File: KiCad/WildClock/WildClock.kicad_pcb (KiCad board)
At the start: 2 copper layers, 70 x 70 mm, 37 parts, among them Q1 AO3401A, Q2 AO3401A, Q3 AO3401A, Q4 AO3401A, Q5 AO3400A, SW1 SWUP, SW2 SWDOWN, SW3 SWOK, U1 ESP32-C3-MINI-1, U3 74HC595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

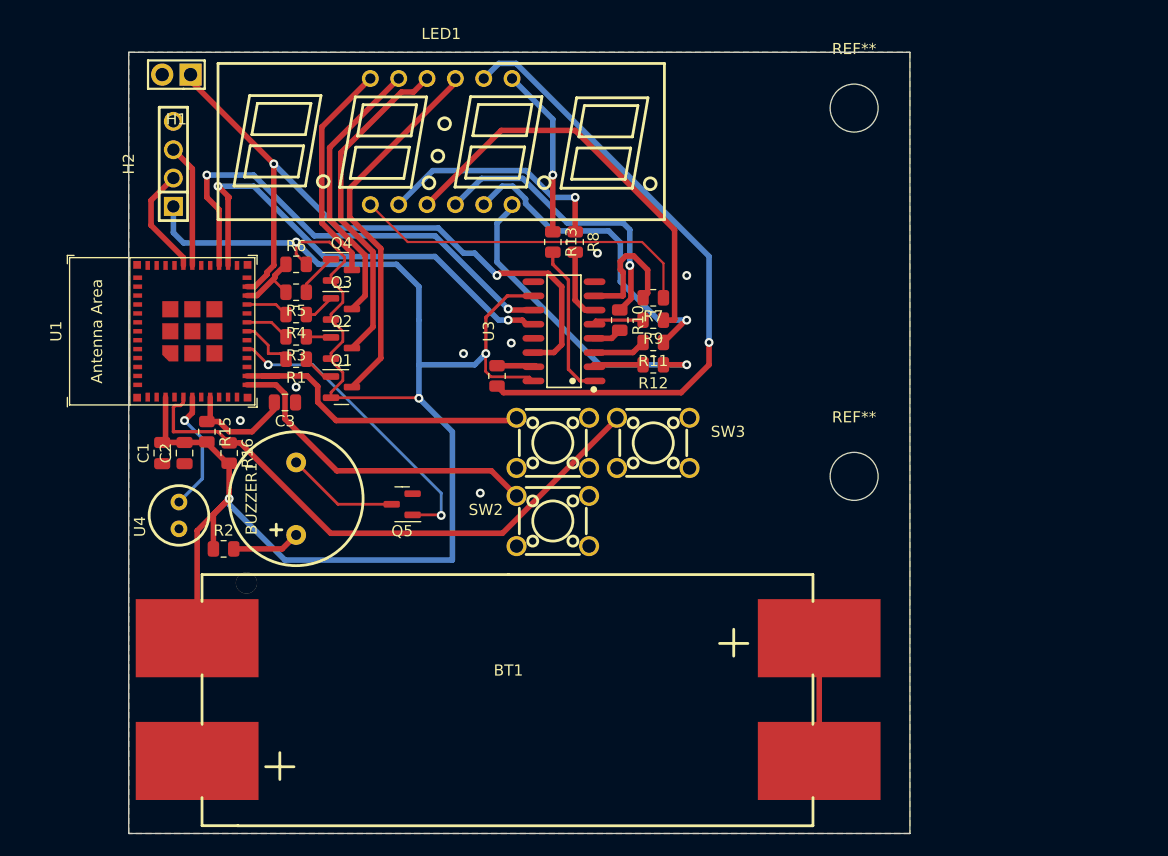
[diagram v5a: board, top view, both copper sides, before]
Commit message: added lables and move everything closer together
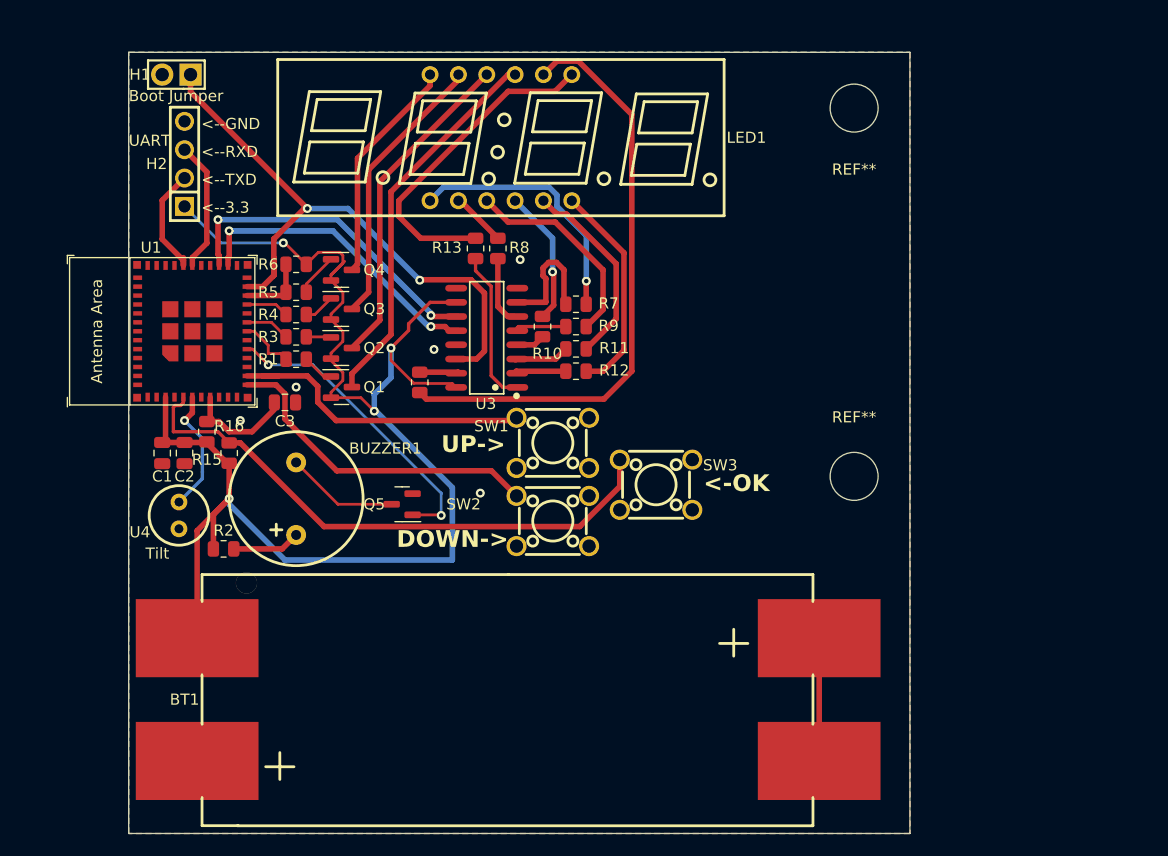
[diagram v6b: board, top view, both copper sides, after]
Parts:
- moved R10 6.95 mm to (60.1, 41.6)
- moved R11 6.95 mm to (63.1, 43.6)
- moved R12 6.95 mm to (63.1, 45.6)
- moved R13 6.95 mm to (54.1, 34.6)
- moved R14 6.95 mm to (49.1, 46.6)
- moved R7 6.95 mm to (63.1, 39.6)
- moved R8 6.95 mm to (56.1, 34.6)
- moved R9 6.95 mm to (63.1, 41.6)
- moved U3 6.95 mm to (55.1, 42.6)
- moved LED1 5.36 mm to (56.4, 24.6)
- moved SW3 3.76 mm to (70.2, 55.8)
- moved H2 1.00 mm to (28.0, 27.0)
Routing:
- net +3.3V: track 160.4 -> 133.6 mm
- net Net-(LED1-C): track 37.8 -> 18.7 mm
- net Net-(LED1-B): track 21.2 -> 4.93 mm, vias 1 -> 0
- net Net-(LED1-G): track 15.2 -> 29.3 mm, vias 1 -> 0
- net RCLK: track 41.2 -> 27.4 mm
- net SRCLK: track 43.1 -> 29.5 mm
- net Net-(LED1-D): track 26.2 -> 12.5 mm
- net Net-(LED1-E): track 28.5 -> 17.6 mm, vias 1 -> 0
- net Net-(LED1-F): track 29.0 -> 19.5 mm, vias 1 -> 0
- net Net-(LED1-A): track 31.5 -> 23.0 mm, vias 0 -> 1
- net SER: track 61.8 -> 55.0 mm
- net Net-(LED1-DI): track 57.9 -> 53.7 mm, vias 1 -> 0
- net RXD0: track 11.1 -> 11.7 mm
- net CA4: track 33.8 -> 34.4 mm
- net GND: vias 7 -> 5
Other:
- board text added: "<--3.3"
- board text added: "<--GND"
- board text added: "<--RXD"
- board text added: "<--TXD"
- board text added: "<-OK"
- board text added: "Boot Jumper"
- board text added: "DOWN->"
- board text added: "Tilt"
- board text added: "UART"
- board text added: "UP->"

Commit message: fix batterie orientation
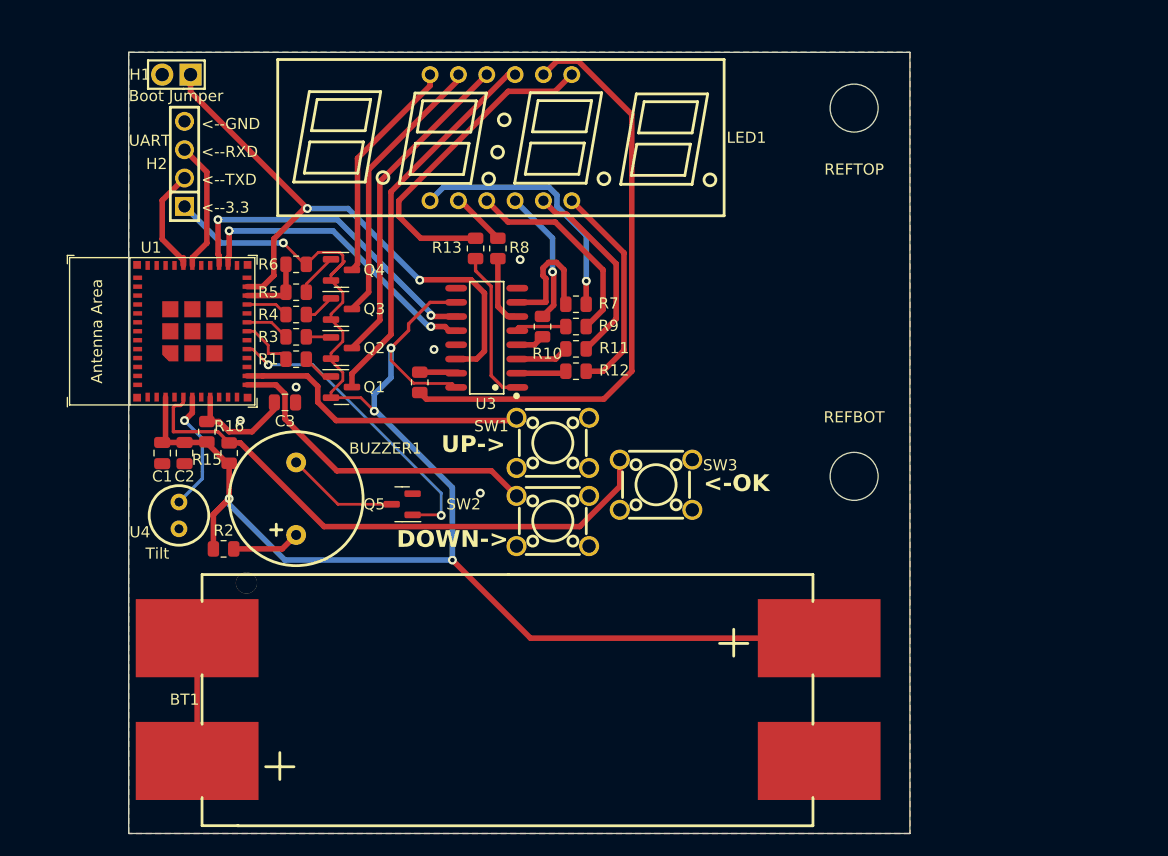
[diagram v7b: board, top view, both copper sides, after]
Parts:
- renumbered REF** to REFBOT, REF** to REFTOP
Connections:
- BT1 pad 1: Net-(BT1-Pad1) -> +3.3V
- BT1 pad 2: +3.3V -> Net-(BT1-Pad2)
- BT1 pad 3: GND -> Net-(BT1-Pad2)
- BT1 pad 4: Net-(BT1-Pad1) -> GND
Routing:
- net +3.3V: track 133.6 -> 157.1 mm, vias 4 -> 5
- net Net-(BT1-Pad2): track 0.00 -> 11.0 mm
- net Net-(BT1-Pad1): track 11.0 -> 0.00 mm
- net SER: track 55.0 -> 53.4 mm
- net SWUP: track 28.1 -> 26.7 mm
- net Q1: track 5.63 -> 4.96 mm
